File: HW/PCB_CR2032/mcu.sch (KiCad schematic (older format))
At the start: 15 parts, among them U1 STM32L071CBTx, Y1 32768 Hz

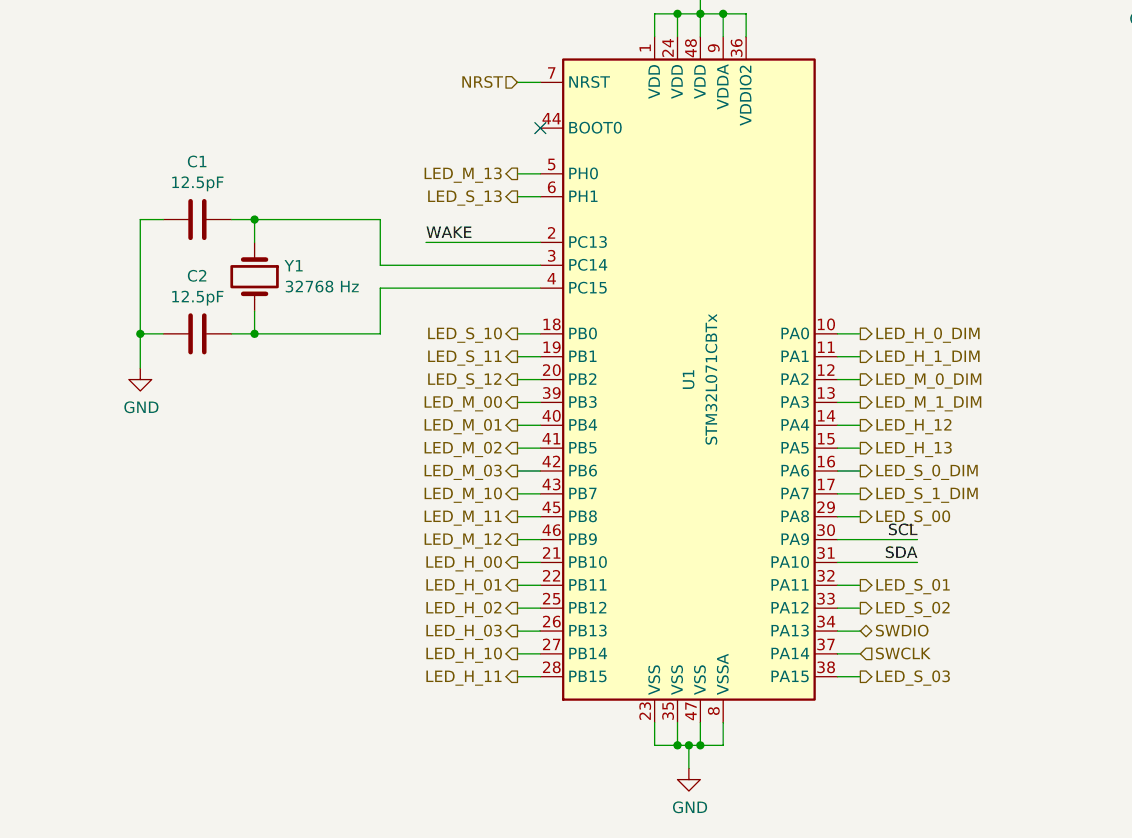
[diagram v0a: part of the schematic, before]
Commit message: * Updated Schematic with 1206 leds and 1k 0805 current limiting resistors
* Restored STDC14 and debug UART, now shared with top led of minute and second. Some other LED pins remapped

* Updated STM32CubeMX project to reflect schematic changes and generated code again
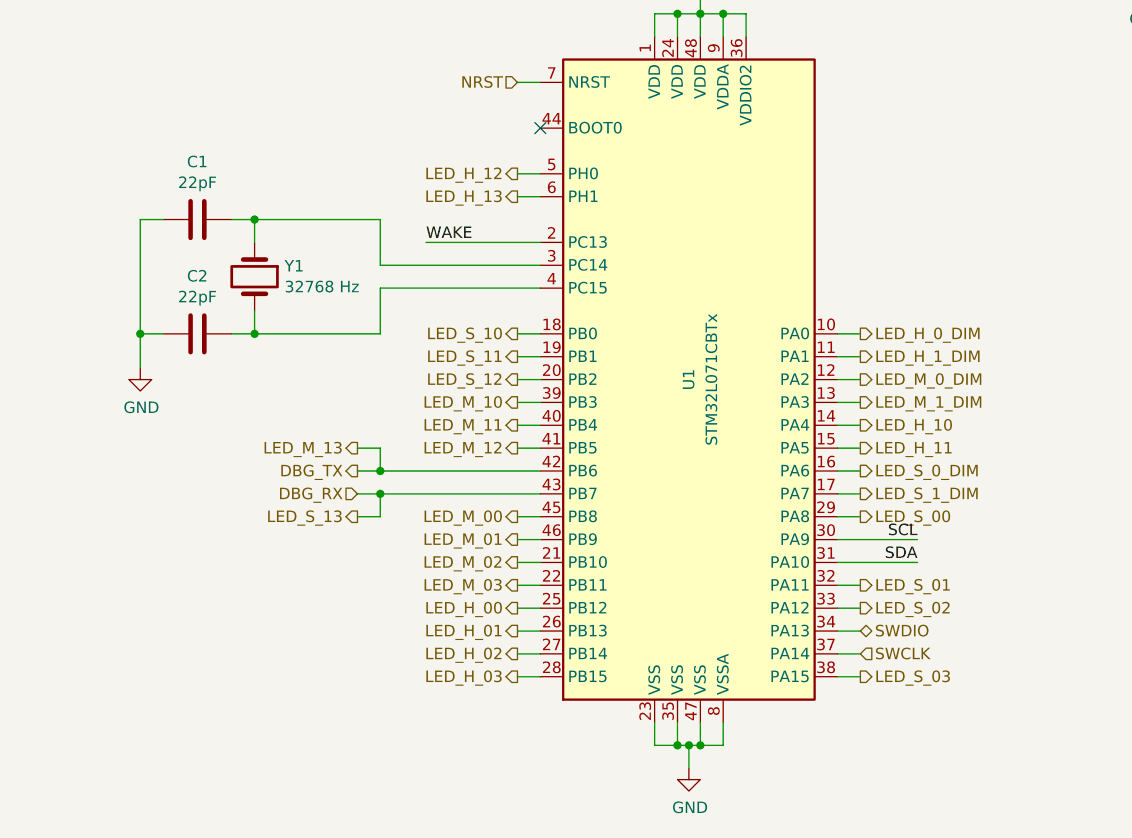
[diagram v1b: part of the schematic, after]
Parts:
- C1, C2: value 12.5pF -> 22pF; Make (none) -> Yageo; Mouser (none) -> 603-CC805JRNPO9BN200; Part (none) -> CC0805JRNPO9BN200
- C15, C4, C5, C6, C7, C8: Make (none) -> Yageo; Mouser (none) -> 603-CC805KRX7R9BB104; Part (none) -> CC0805KRX7R9BB104
- C3: Make Murata -> Yageo; Mouser 81-GRM21BR71A106KA73K -> 603-CC805KKX7R6BB106; Part GRM21BR71A106KA73K -> CC0805KKX7R6BB106
- R28, R29, R30, R31: Make (none) -> Yageo; Mouser (none) -> 603-RC0805FR-0710KL; Part (none) -> RC0805FR-0710KL
- U1: Make (none) -> ST; Mouser (none) -> 511-STM32L071CBT6TR; Part (none) -> STM32L071CBT6
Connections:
- net LED_M_13 is gone; now on net LED_H_12: U1.5 (PH0)
- net LED_S_13 is gone; now on net LED_H_13: U1.6 (PH1)
- net LED_H_00: now also U1.25 (PB12); no longer U1.21 (PB10)
- net LED_H_01: now also U1.26 (PB13); no longer U1.22 (PB11)
- net LED_H_02: now also U1.27 (PB14); no longer U1.25 (PB12)
- net LED_H_03: now also U1.28 (PB15); no longer U1.26 (PB13)
- net LED_H_10: now also U1.14 (PA4); no longer U1.27 (PB14)
- net LED_H_11: now also U1.15 (PA5); no longer U1.28 (PB15)
- net LED_H_12: no longer U1.14 (PA4)
- net LED_H_13: no longer U1.15 (PA5)
- net LED_M_00: now also U1.45 (PB8); no longer U1.39 (PB3)
- net LED_M_01: now also U1.46 (PB9); no longer U1.40 (PB4)
- net LED_M_02: now also U1.21 (PB10); no longer U1.41 (PB5)
- net LED_M_03: now also U1.22 (PB11); no longer U1.42 (PB6)
- net LED_M_10: now also U1.39 (PB3); no longer U1.43 (PB7)
- net LED_M_11: now also U1.40 (PB4); no longer U1.45 (PB8)
- net LED_M_12: now also U1.41 (PB5); no longer U1.46 (PB9)
- new net DBG_RX: U1.43 (PB7)
- new net DBG_TX: U1.42 (PB6)
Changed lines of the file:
@@
 Text HLabel 9450 4250 2    50   Input ~ 0
 WAKE_UP
+Text HLabel 6250 3800 2    50   Output ~ 0
+LED_H_11
+Text HLabel 6250 3700 2    50   Output ~ 0
+LED_H_10
 Text HLabel 4750 4800 0    50   Output ~ 0
-LED_H_11
+LED_H_03
 Text HLabel 4750 4700 0    50   Output ~ 0
-LED_H_10
+LED_H_02
 Text HLabel 4750 4600 0    50   Output ~ 0
-LED_H_03
+LED_H_01
 Text HLabel 4750 4500 0    50   Output ~ 0
-LED_H_02
+LED_H_00
+Text HLabel 4750 3800 0    50   Output ~ 0
+LED_M_12
+Text HLabel 4750 3700 0    50   Output ~ 0
+LED_M_11
+Text HLabel 4750 3600 0    50   Output ~ 0
+LED_M_10
 Text HLabel 4750 4400 0    50   Output ~ 0
-LED_H_01
+LED_M_03
 Text HLabel 4750 4300 0    50   Output ~ 0
-LED_H_00
+LED_M_02
 Text HLabel 4750 4200 0    50   Output ~ 0
-LED_M_12
+LED_M_01
 Text HLabel 4750 4100 0    50   Output ~ 0
-LED_M_11
-Text HLabel 4750 4000 0    50   Output ~ 0
-LED_M_10
-Text HLabel 4750 3900 0    50   Output ~ 0
-LED_M_03
-Text HLabel 4750 3800 0    50   Output ~ 0
-LED_M_02
-Text HLabel 4750 3700 0    50   Output ~ 0
-LED_M_01
-Text HLabel 4750 3600 0    50   Output ~ 0
 LED_M_00
 Text HLabel 4750 3500 0    50   Output ~ 0
@@
 F 2 "Package_QFP:LQFP-48_7x7mm_P0.5mm" H 4950 2100 50  0001 R CNN
 F 3 "http://www.st.com/st-web-ui/static/active/en/resource/technical/document/datasheet/DM00141136.pdf" H 5550 3500 50  0001 C CNN
+F 4 "ST" H 5550 3500 50  0001 C CNN "Make"
+F 5 "511-STM32L071CBT6TR" H 5550 3500 50  0001 C CNN "Mouser"
+F 6 "STM32L071CBT6" H 5550 3500 50  0001 C CNN "Part"
 	1    5550 3500
 	1    0    0    -1
@@
 	4850 3800 4750 3800
 Wire Wire Line
-	4850 3900 4750 3900
-Wire Wire Line
-	4850 4000 4750 4000
-Wire Wire Line
 	4850 4100 4750 4100
 Wire Wire Line
@@
 F 2 "Capacitor_SMD:C_0805_2012Metric_Pad1.15x1.40mm_HandSolder" H 8238 1350 50  0001 C CNN
 F 3 "~" H 8200 1500 50  0001 C CNN
+F 4 "Yageo" H 8200 1500 50  0001 C CNN "Make"
+F 5 "603-CC805KRX7R9BB104" H 8200 1500 50  0001 C CNN "Mouser"
+F 6 "CC0805KRX7R9BB104" H 8200 1500 50  0001 C CNN "Part"
 	1    8200 1500
 	1    0    0    -1
@@
 F 2 "Capacitor_SMD:C_0805_2012Metric_Pad1.15x1.40mm_HandSolder" H 7538 1350 50  0001 C CNN
 F 3 "~" H 7500 1500 50  0001 C CNN
-F 4 "Murata" H 7500 1500 50  0001 C CNN "Make"
-F 5 "GRM21BR71A106KA73K" H 7500 1500 50  0001 C CNN "Part"
-F 6 "81-GRM21BR71A106KA73K" H 7500 1500 50  0001 C CNN "Mouser"
+F 4 "Yageo" H 7500 1500 50  0001 C CNN "Make"
+F 5 "CC0805KKX7R6BB106" H 7500 1500 50  0001 C CNN "Part"
+F 6 "603-CC805KKX7R6BB106" H 7500 1500 50  0001 C CNN "Mouser"
 	1    7500 1500
 	1    0    0    -1
@@
 F 2 "Capacitor_SMD:C_0805_2012Metric_Pad1.15x1.40mm_HandSolder" H 8788 1350 50  0001 C CNN
 F 3 "~" H 8750 1500 50  0001 C CNN
+F 4 "Yageo" H 8750 1500 50  0001 C CNN "Make"
+F 5 "603-CC805KRX7R9BB104" H 8750 1500 50  0001 C CNN "Mouser"
+F 6 "CC0805KRX7R9BB104" H 8750 1500 50  0001 C CNN "Part"
 	1    8750 1500
 	1    0    0    -1
@@
 F 2 "Capacitor_SMD:C_0805_2012Metric_Pad1.15x1.40mm_HandSolder" H 9338 1350 50  0001 C CNN
 F 3 "~" H 9300 1500 50  0001 C CNN
+F 4 "Yageo" H 9300 1500 50  0001 C CNN "Make"
+F 5 "603-CC805KRX7R9BB104" H 9300 1500 50  0001 C CNN "Mouser"
+F 6 "CC0805KRX7R9BB104" H 9300 1500 50  0001 C CNN "Part"
 	1    9300 1500
 	1    0    0    -1
@@
 F 2 "Capacitor_SMD:C_0805_2012Metric_Pad1.15x1.40mm_HandSolder" H 9888 1350 50  0001 C CNN
 F 3 "~" H 9850 1500 50  0001 C CNN
+F 4 "Yageo" H 9850 1500 50  0001 C CNN "Make"
+F 5 "603-CC805KRX7R9BB104" H 9850 1500 50  0001 C CNN "Mouser"
+F 6 "CC0805KRX7R9BB104" H 9850 1500 50  0001 C CNN "Part"
 	1    9850 1500
 	1    0    0    -1
@@
 F 2 "Capacitor_SMD:C_0805_2012Metric_Pad1.15x1.40mm_HandSolder" H 10438 1350 50  0001 C CNN
 F 3 "~" H 10400 1500 50  0001 C CNN
+F 4 "Yageo" H 10400 1500 50  0001 C CNN "Make"
+F 5 "603-CC805KRX7R9BB104" H 10400 1500 50  0001 C CNN "Mouser"
+F 6 "CC0805KRX7R9BB104" H 10400 1500 50  0001 C CNN "Part"
 	1    10400 1500
 	1    0    0    -1
@@
 	6250 4000 6150 4000
 NoConn ~ 750  3850
-Text HLabel 6250 3700 2    50   Output ~ 0
+Text HLabel 4750 2600 0    50   Output ~ 0
 LED_H_12
-Text HLabel 6250 3800 2    50   Output ~ 0
+Text HLabel 4750 2700 0    50   Output ~ 0
 LED_H_13
-Text HLabel 4750 2600 0    50   Output ~ 0
+Text HLabel 4050 3800 0    50   Output ~ 0
 LED_M_13
-Text HLabel 4750 2700 0    50   Output ~ 0
+Text HLabel 4050 4100 0    50   Output ~ 0
 LED_S_13
 Text HLabel 9450 4050 2    50   BiDi ~ 0
@@
 P 3350 3300
 F 0 "C2" V 3098 3300 50  0000 C CNN
-F 1 "12.5pF" V 3189 3300 50  0000 C CNN
+F 1 "22pF" V 3189 3300 50  0000 C CNN
 F 2 "Capacitor_SMD:C_0805_2012Metric_Pad1.15x1.40mm_HandSolder" H 3388 3150 50  0001 C CNN
 F 3 "~" H 3350 3300 50  0001 C CNN
+F 4 "Yageo" H 3350 3300 50  0001 C CNN "Make"
+F 5 "603-CC805JRNPO9BN200" H 3350 3300 50  0001 C CNN "Mouser"
+F 6 "CC0805JRNPO9BN200" H 3350 3300 50  0001 C CNN "Part"
 	1    3350 3300
 	0    1    1    0
@@
 P 3350 2800
 F 0 "C1" V 3098 2800 50  0000 C CNN
-F 1 "12.5pF" V 3189 2800 50  0000 C CNN
+F 1 "22pF" V 3189 2800 50  0000 C CNN
 F 2 "Capacitor_SMD:C_0805_2012Metric_Pad1.15x1.40mm_HandSolder" H 3388 2650 50  0001 C CNN
 F 3 "~" H 3350 2800 50  0001 C CNN
+F 4 "Yageo" H 3350 2800 50  0001 C CNN "Make"
+F 5 "603-CC805JRNPO9BN200" H 3350 2800 50  0001 C CNN "Mouser"
+F 6 "CC0805JRNPO9BN200" H 3350 2800 50  0001 C CNN "Part"
 	1    3350 2800
 	0    1    1    0
@@
 F 2 "Resistor_SMD:R_0805_2012Metric_Pad1.15x1.40mm_HandSolder" V 8680 4500 50  0001 C CNN
 F 3 "~" H 8750 4500 50  0001 C CNN
+F 4 "Yageo" H 8750 4500 50  0001 C CNN "Make"
+F 5 "603-RC0805FR-0710KL" H 8750 4500 50  0001 C CNN "Mouser"
+F 6 "RC0805FR-0710KL" H 8750 4500 50  0001 C CNN "Part"
 	1    8750 4500
 	1    0    0    -1
@@
 F 2 "Resistor_SMD:R_0805_2012Metric_Pad1.15x1.40mm_HandSolder" V 9280 3700 50  0001 C CNN
 F 3 "~" H 9350 3700 50  0001 C CNN
+F 4 "Yageo" H 9350 3700 50  0001 C CNN "Make"
+F 5 "603-RC0805FR-0710KL" H 9350 3700 50  0001 C CNN "Mouser"
+F 6 "RC0805FR-0710KL" H 9350 3700 50  0001 C CNN "Part"
 	1    9350 3700
 	1    0    0    -1
@@
 F 2 "Resistor_SMD:R_0805_2012Metric_Pad1.15x1.40mm_HandSolder" V 9030 3700 50  0001 C CNN
 F 3 "~" H 9100 3700 50  0001 C CNN
+F 4 "Yageo" H 9100 3700 50  0001 C CNN "Make"
+F 5 "603-RC0805FR-0710KL" H 9100 3700 50  0001 C CNN "Mouser"
+F 6 "RC0805FR-0710KL" H 9100 3700 50  0001 C CNN "Part"
 	1    9100 3700
 	1    0    0    -1
@@
 F 2 "Resistor_SMD:R_0805_2012Metric_Pad1.15x1.40mm_HandSolder" V 9130 4250 50  0001 C CNN
 F 3 "~" H 9200 4250 50  0001 C CNN
+F 4 "Yageo" H 9200 4250 50  0001 C CNN "Make"
+F 5 "603-RC0805FR-0710KL" H 9200 4250 50  0001 C CNN "Mouser"
+F 6 "RC0805FR-0710KL" H 9200 4250 50  0001 C CNN "Part"
 	1    9200 4250
 	0    1    1    0
@@
 F 2 "Capacitor_SMD:C_0805_2012Metric_Pad1.15x1.40mm_HandSolder" H 8988 4350 50  0001 C CNN
 F 3 "~" H 8950 4500 50  0001 C CNN
+F 4 "Yageo" H 8950 4500 50  0001 C CNN "Make"
+F 5 "603-CC805KRX7R9BB104" H 8950 4500 50  0001 C CNN "Mouser"
+F 6 "CC0805KRX7R9BB104" H 8950 4500 50  0001 C CNN "Part"
 	1    8950 4500
 	1    0    0    -1
@@
 Wire Wire Line
 	4350 2900 4850 2900
+Text HLabel 4050 3900 0    50   Output ~ 0
+DBG_TX
+Text HLabel 4050 4000 0    50   Input ~ 0
+DBG_RX
+Wire Wire Line
+	4050 3900 4150 3900
+Wire Wire Line
+	4050 4000 4150 4000
+Wire Wire Line
+	4050 3800 4150 3800
+Wire Wire Line
+	4150 3800 4150 3900
+Connection ~ 4150 3900
+Wire Wire Line
+	4150 3900 4850 3900
+Wire Wire Line
+	4050 4100 4150 4100
+Wire Wire Line
+	4150 4100 4150 4000
+Connection ~ 4150 4000
+Wire Wire Line
+	4150 4000 4850 4000
 $EndSCHEMATC

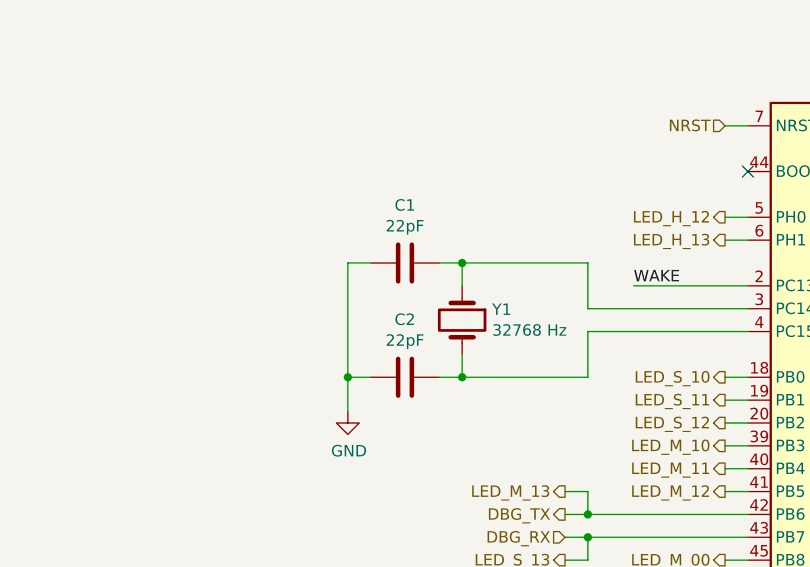
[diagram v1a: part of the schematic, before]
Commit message: * Corrected LED references in schematic
* Corrected value of oscillator load capacitors

* Added HW readme with BoM
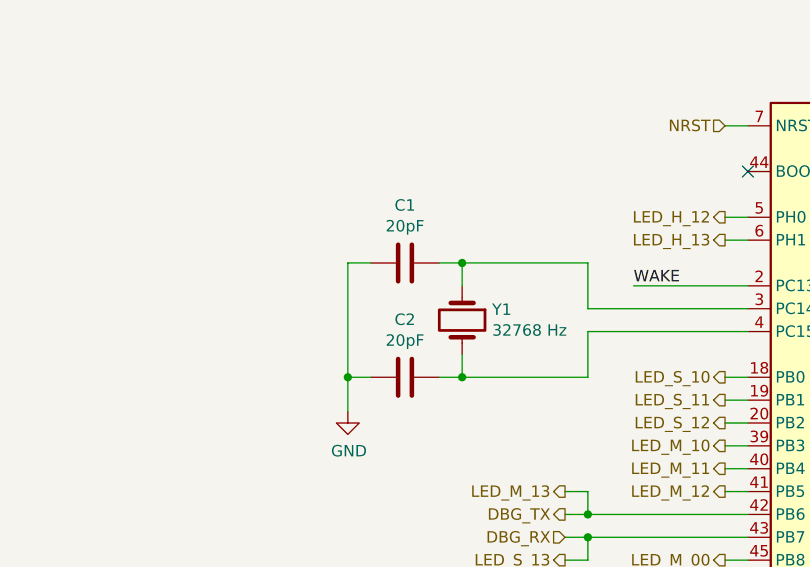
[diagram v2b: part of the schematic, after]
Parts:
- C1, C2: value 22pF -> 20pF
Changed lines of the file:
@@
 P 3350 3300
 F 0 "C2" V 3098 3300 50  0000 C CNN
-F 1 "22pF" V 3189 3300 50  0000 C CNN
+F 1 "20pF" V 3189 3300 50  0000 C CNN
 F 2 "Capacitor_SMD:C_0805_2012Metric_Pad1.15x1.40mm_HandSolder" H 3388 3150 50  0001 C CNN
 F 3 "~" H 3350 3300 50  0001 C CNN
@@
 P 3350 2800
 F 0 "C1" V 3098 2800 50  0000 C CNN
-F 1 "22pF" V 3189 2800 50  0000 C CNN
+F 1 "20pF" V 3189 2800 50  0000 C CNN
 F 2 "Capacitor_SMD:C_0805_2012Metric_Pad1.15x1.40mm_HandSolder" H 3388 2650 50  0001 C CNN
 F 3 "~" H 3350 2800 50  0001 C CNN
